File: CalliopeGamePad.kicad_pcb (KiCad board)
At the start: 2 copper layers, 134 x 42 mm, 28 parts, among them J1 Conn_02x15_Odd_Even, J2 Conn_01x04, U1 SW_MEC_5E, U2 SW_MEC_5E, U3 SW_MEC_5E, U4 SW_MEC_5E, U5 SW_MEC_5E, U6 SW_MEC_5E, U7 SW_MEC_5E, U8 SW_MEC_5E

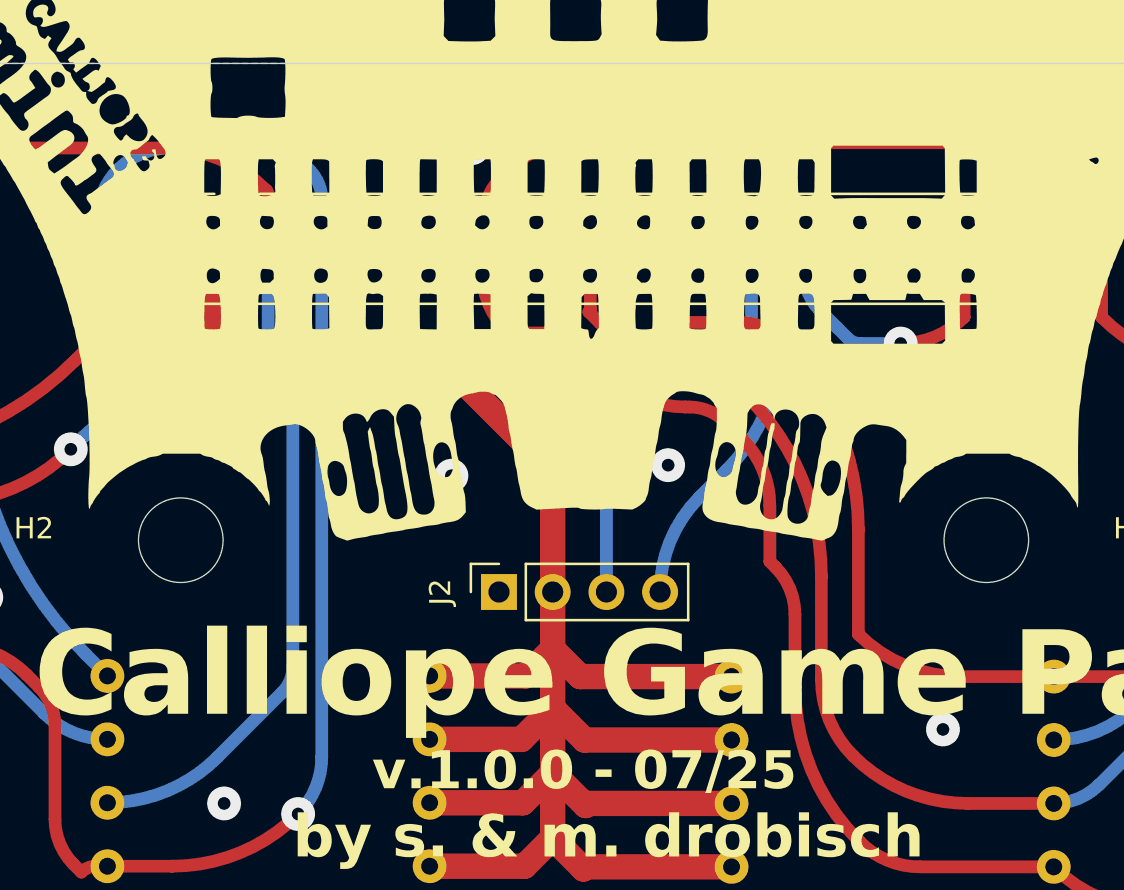
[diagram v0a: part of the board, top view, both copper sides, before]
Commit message: MAKE the socket a pin header and reroute pin map
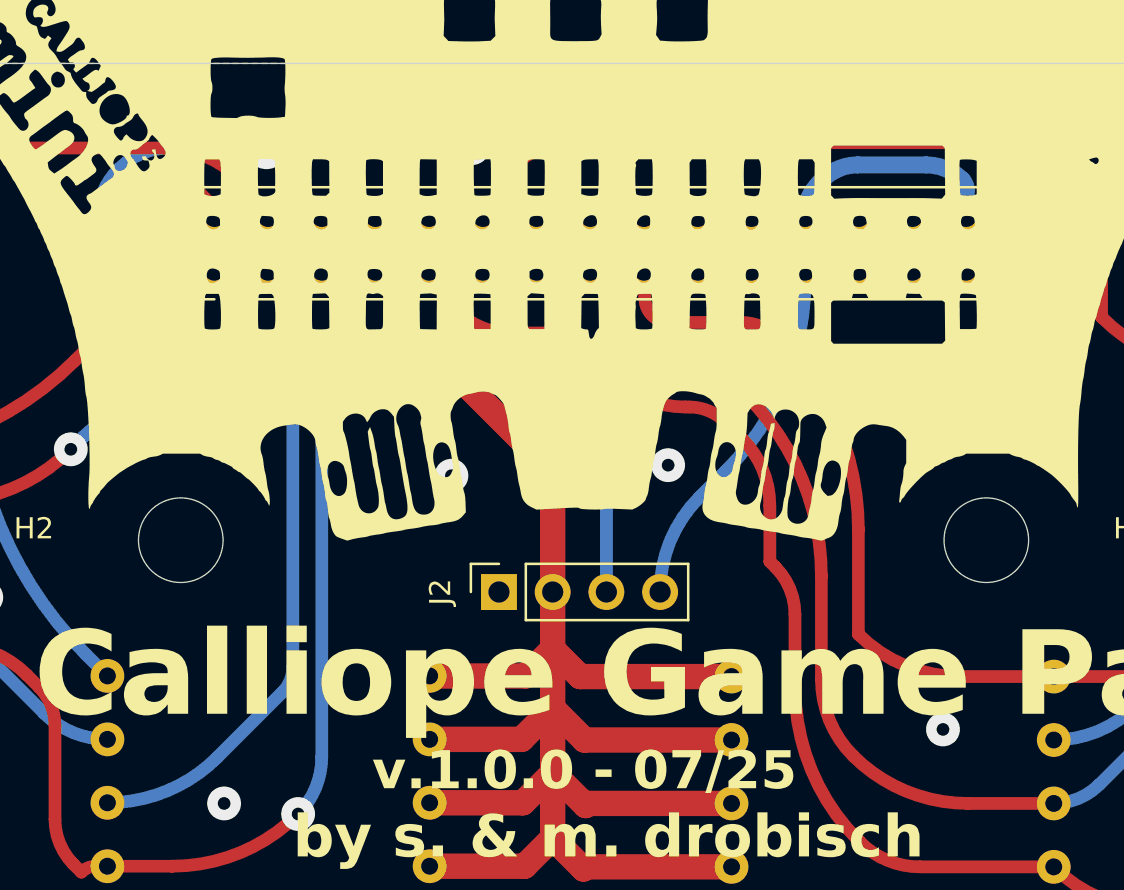
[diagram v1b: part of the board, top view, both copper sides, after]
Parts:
- J1: footprint Connector_PinSocket_2.54mm:PinSocket_2x15_P2.54mm_Vertical -> Connector_PinHeader_2.54mm:PinHeader_2x15_P2.54mm_Vertical
- moved J1 2.28 mm to (132.5, 94.8)
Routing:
- net +3.3V: track 101.7 -> 111.2 mm
- net /C9: track 106.4 -> 111.1 mm
- net /P1: track 76.0 -> 79.9 mm
- net /P3: track 71.3 -> 75.2 mm, vias 1 -> 2
- net /SDA: track 20.7 -> 17.2 mm
- net /SCL: track 18.7 -> 21.3 mm
- net /C8: track 84.5 -> 86.9 mm
- net /C13: track 69.8 -> 72.0 mm
- net /P2: track 61.6 -> 63.7 mm, vias 1 -> 2
- net /P0: track 70.6 -> 72.5 mm
- net /C14: track 71.2 -> 69.6 mm
- net GND: track 11.5 -> 10.7 mm
